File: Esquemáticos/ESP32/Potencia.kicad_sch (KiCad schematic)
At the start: 12 parts, among them J3 Barrel_Jack, SW1 SW_DIP_x01, U5 AMS1117-5.0, U6 AMS1117-3.3

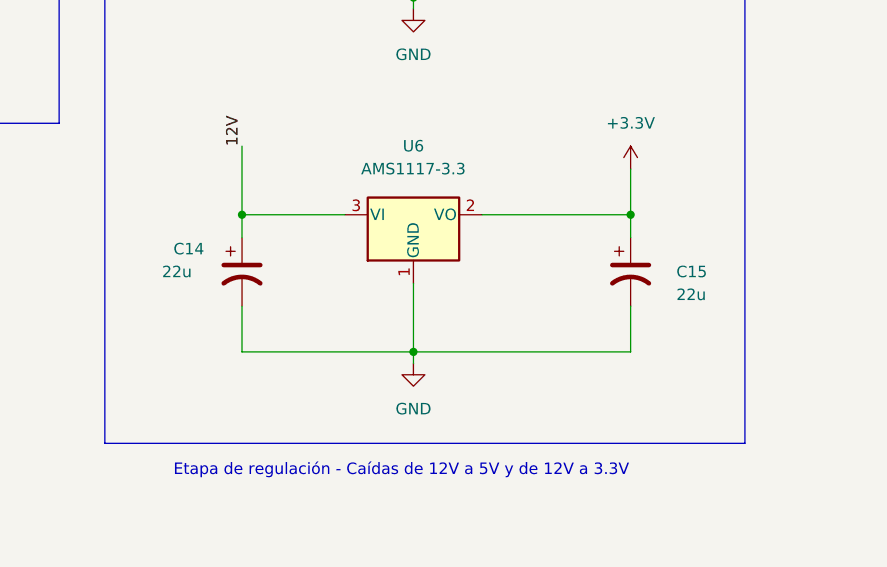
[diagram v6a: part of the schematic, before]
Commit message: Ruteo y zonas de cobre. Modo_serio.jpg
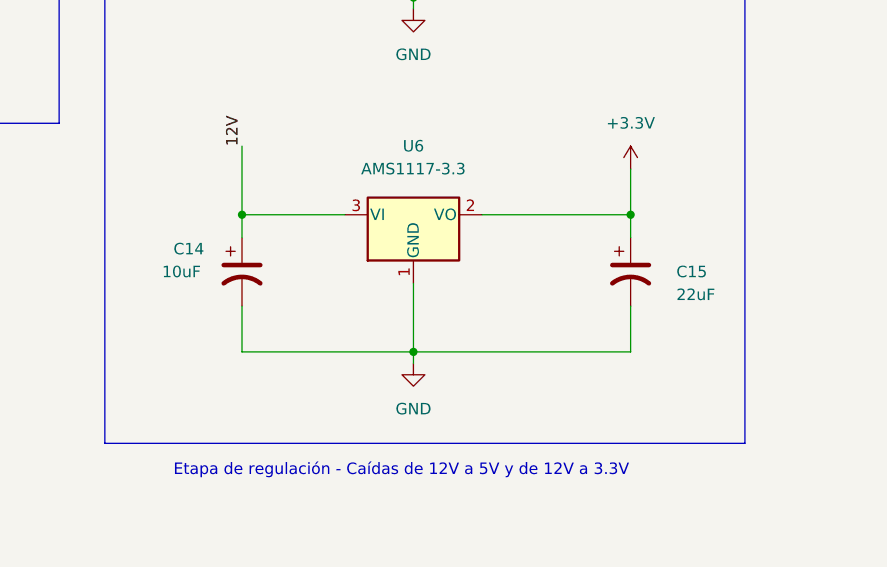
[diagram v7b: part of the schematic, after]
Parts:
- C14: value 22u -> 10uF
- C15: value 22u -> 22uF
- D3: footprint Diode_THT:D_DO-41_SOD81_P10.16mm_Horizontal -> Diode_SMD:D_SMA_Handsoldering
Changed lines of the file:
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@@
     (property "Reference" "D3" (id 0) (at 109.22 82.55 0))
     (property "Value" "1N4007" (id 1) (at 109.22 85.09 0))
-    (property "Footprint" "Diode_THT:D_DO-41_SOD81_P10.16mm_Horizontal" (id 2) (at 109.22 84.455 0)
+    (property "Footprint" "Diode_SMD:D_SMA_Handsoldering" (id 2) (at 109.22 84.455 0)
       (effects (font (size 1.27 1.27)) hide)
     )
@@
       (effects (font (size 1.27 1.27)) (justify left))
     )
-    (property "Value" "22u" (id 1) (at 212.09 137.16 0)
+    (property "Value" "22uF" (id 1) (at 212.09 137.16 0)
       (effects (font (size 1.27 1.27)) (justify left))
     )
@@
       (effects (font (size 1.27 1.27)) (justify left))
     )
-    (property "Value" "22u" (id 1) (at 154.94 134.62 0)
+    (property "Value" "10uF" (id 1) (at 154.94 134.62 0)
       (effects (font (size 1.27 1.27)) (justify left))
     )

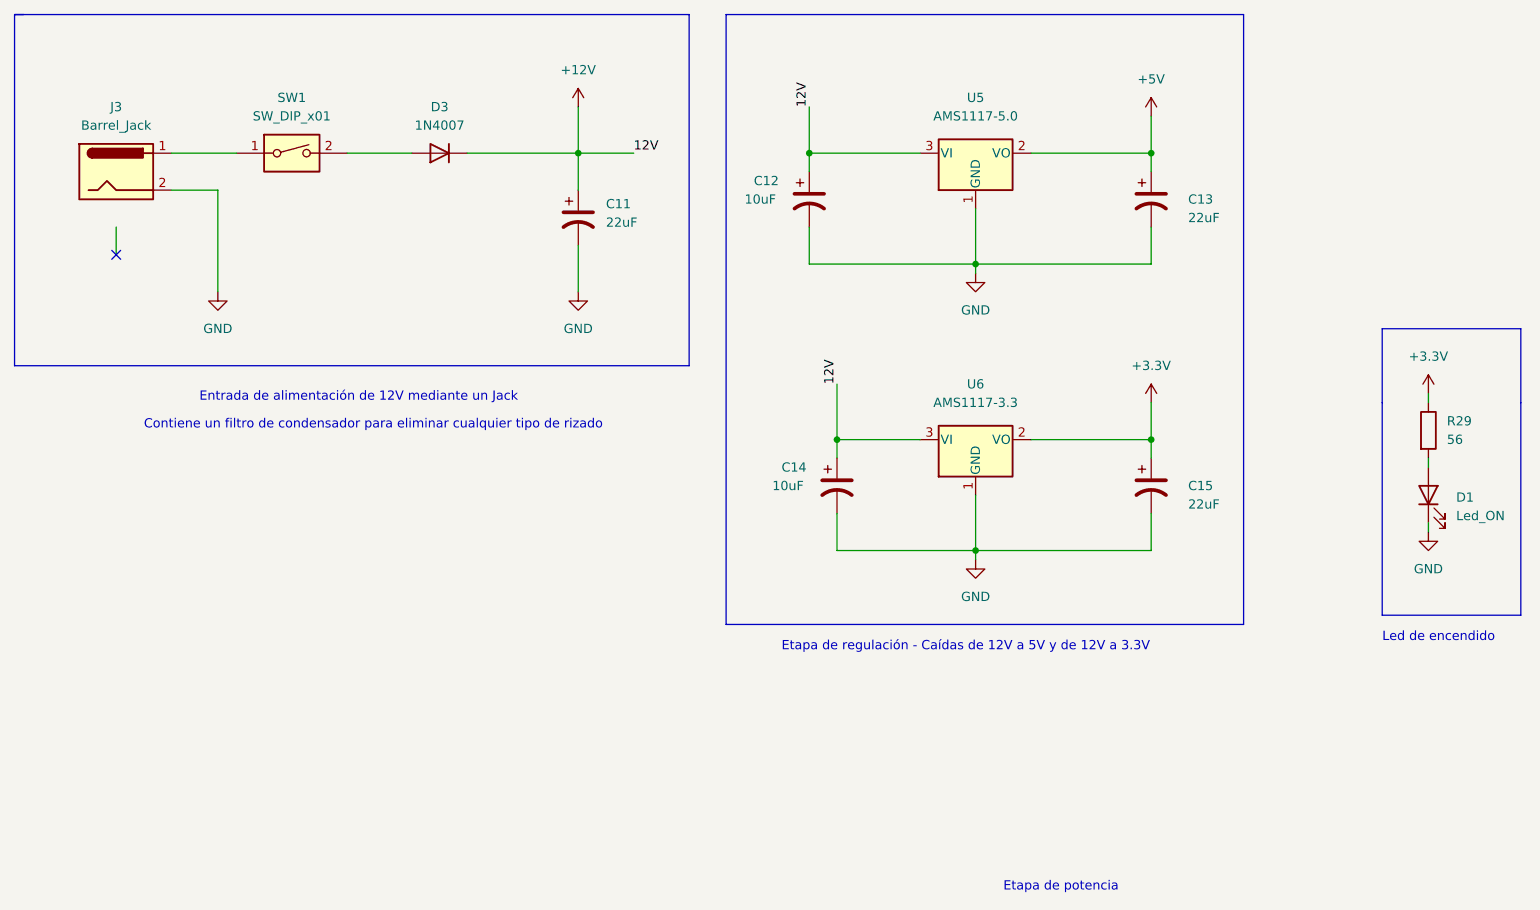
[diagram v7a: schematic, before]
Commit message: Huellas actualizadas según los vendedores locales
Falta la del optoacoplador y actualizar la placa. Además, dependiendo de la resñpuesta del profe tocaría re-diseñar todo :c
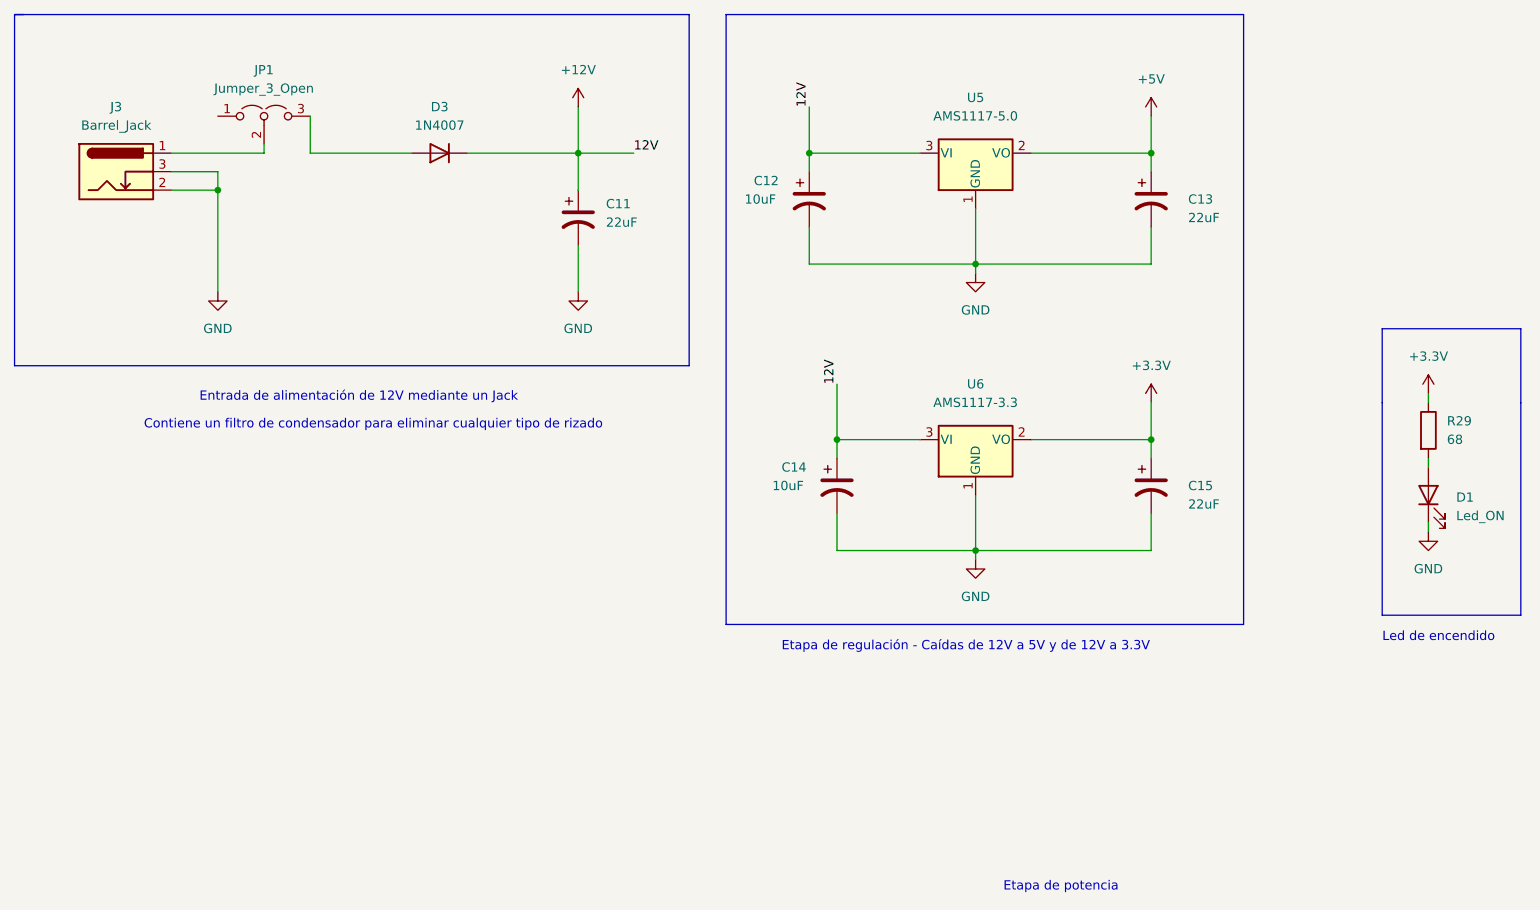
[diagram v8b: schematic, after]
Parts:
- removed SW1: SW_DIP_x01, Button_Switch_SMD:SW_DIP_SPSTx01_Slide_6.7x4.1mm_W6.73mm_P2.54mm_LowProfile_JPin, symbol Switch:SW_DIP_x01
- added JP1: Jumper_3_Open, Connector_PinHeader_2.54mm:PinHeader_1x03_P2.54mm_Vertical, symbol Jumper:Jumper_3_Open
- C11, C12, C13, C14, C15: footprint Capacitor_SMD:C_0603_1608Metric_Pad1.08x0.95mm_HandSolder -> Capacitor_SMD:C_0805_2012Metric_Pad1.18x1.45mm_HandSolder
- J3: footprint Connector_BarrelJack:BarrelJack_CLIFF_FC681465S_SMT_Horizontal -> Connector_BarrelJack:BarrelJack_GCT_DCJ200-10-A_Horizontal; symbol Connector:Barrel_Jack -> Connector:Barrel_Jack_Switch
- R29: value 56 -> 68; footprint Resistor_SMD:R_0603_1608Metric_Pad0.98x0.95mm_HandSolder -> Resistor_SMD:R_1206_3216Metric_Pad1.30x1.75mm_HandSolder
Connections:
- net GND: now also J3.3
- net at J3.1: now also JP1.2 (C)
- net at D3.2 (A): now also JP1.3 (B)
- no-connect marks 1 -> 0
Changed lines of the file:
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@@
 (kicad_sch (version 20211123) (generator eeschema)
   (paper "A4")
+  (junction (at 78.74 93.98) (diameter 0) (color 0 0 0 0)
+  )
   (junction (at 160.02 88.9) (diameter 0) (color 0 0 0 0)
   )
@@
   (junction (at 182.88 104.14) (diameter 0) (color 0 0 0 0)
   )
-  (no_connect (at 64.77 102.87))
   (wire (pts (xy 182.88 104.14) (xy 207.01 104.14))
     (stroke (width 0) (type default) (color 0 0 0 0))
@@
     (stroke (width 0) (type default) (color 0 0 0 0))
   )
-  (wire (pts (xy 72.39 88.9) (xy 81.28 88.9))
+  (wire (pts (xy 72.39 88.9) (xy 85.09 88.9))
     (stroke (width 0) (type default) (color 0 0 0 0))
   )
@@
     (stroke (width 0) (type default) (color 0 0 0 0))
   )
+  (wire (pts (xy 91.44 83.82) (xy 91.44 88.9))
+    (stroke (width 0) (type default) (color 0 0 0 0))
+  )
   (wire (pts (xy 245.11 130.81) (xy 245.11 132.08))
     (stroke (width 0) (type default) (color 0 0 0 0))
@@
     (stroke (width 0) (type default) (color 0 0 0 0))
   )
-  (wire (pts (xy 64.77 102.87) (xy 64.77 99.06))
-    (stroke (width 0) (type default) (color 0 0 0 0))
-  )
   (polyline (pts (xy 219.71 153.67) (xy 219.71 69.85))
     (stroke (width 0) (type default) (color 0 0 0 0))
@@
     (stroke (width 0) (type default) (color 0 0 0 0))
   )
+  (wire (pts (xy 85.09 87.63) (xy 85.09 88.9))
+    (stroke (width 0) (type default) (color 0 0 0 0))
+  )
   (wire (pts (xy 245.11 139.7) (xy 245.11 140.97))
     (stroke (width 0) (type default) (color 0 0 0 0))
@@
     (stroke (width 0) (type default) (color 0 0 0 0))
   )
-  (wire (pts (xy 96.52 88.9) (xy 105.41 88.9))
+  (wire (pts (xy 91.44 88.9) (xy 105.41 88.9))
     (stroke (width 0) (type default) (color 0 0 0 0))
   )
@@
     (stroke (width 0) (type default) (color 0 0 0 0))
   )
+  (wire (pts (xy 72.39 91.44) (xy 78.74 91.44))
+    (stroke (width 0) (type default) (color 0 0 0 0))
+  )
   (polyline (pts (xy 238.76 113.03) (xy 257.81 113.03))
     (stroke (width 0) (type default) (color 0 0 0 0))
@@
   )
   (polyline (pts (xy 257.81 113.03) (xy 257.81 123.19))
+    (stroke (width 0) (type default) (color 0 0 0 0))
+  )
+  (wire (pts (xy 78.74 91.44) (xy 78.74 93.98))
     (stroke (width 0) (type default) (color 0 0 0 0))
   )
@@
       (effects (font (size 1.27 1.27)) (justify left))
     )
-    (property "Footprint" "Capacitor_SMD:C_0603_1608Metric_Pad1.08x0.95mm_HandSolder" (id 2) (at 207.01 95.25 0)
+    (property "Footprint" "Capacitor_SMD:C_0805_2012Metric_Pad1.18x1.45mm_HandSolder" (id 2) (at 207.01 95.25 0)
       (effects (font (size 1.27 1.27)) hide)
     )
@@
       (effects (font (size 1.27 1.27)) (justify left))
     )
-    (property "Footprint" "Capacitor_SMD:C_0603_1608Metric_Pad1.08x0.95mm_HandSolder" (id 2) (at 160.02 95.25 0)
+    (property "Footprint" "Capacitor_SMD:C_0805_2012Metric_Pad1.18x1.45mm_HandSolder" (id 2) (at 160.02 95.25 0)
       (effects (font (size 1.27 1.27)) hide)
     )
@@
     (pin "2")
   )
-  (symbol (lib_id "Connector:Barrel_Jack") (at 64.77 91.44 0) (unit 1)
+  (symbol (lib_id "Connector:Barrel_Jack_Switch") (at 64.77 91.44 0) (unit 1)
     (in_bom yes) (on_board yes) (fields_autoplaced)
     (property "Reference" "J3" (id 0) (at 64.77 82.55 0))
     (property "Value" "Barrel_Jack" (id 1) (at 64.77 85.09 0))
-    (property "Footprint" "Connector_BarrelJack:BarrelJack_CLIFF_FC681465S_SMT_Horizontal" (id 2) (at 66.04 92.456 0)
+    (property "Footprint" "Connector_BarrelJack:BarrelJack_GCT_DCJ200-10-A_Horizontal" (id 2) (at 66.04 92.456 0)
       (effects (font (size 1.27 1.27)) hide)
     )
@@
     (pin "1")
     (pin "2")
+    (pin "3")
   )
   (symbol (lib_id "Diode:1N4007") (at 109.22 88.9 180) (unit 1)
@@
       (effects (font (size 1.27 1.27)) (justify left))
     )
-    (property "Footprint" "Capacitor_SMD:C_0603_1608Metric_Pad1.08x0.95mm_HandSolder" (id 2) (at 207.01 134.62 0)
+    (property "Footprint" "Capacitor_SMD:C_0805_2012Metric_Pad1.18x1.45mm_HandSolder" (id 2) (at 207.01 134.62 0)
       (effects (font (size 1.27 1.27)) hide)
     )
@@
       (effects (font (size 1.27 1.27)) (justify left))
     )
-    (property "Footprint" "Capacitor_SMD:C_0603_1608Metric_Pad1.08x0.95mm_HandSolder" (id 2) (at 163.83 134.62 0)
+    (property "Footprint" "Capacitor_SMD:C_0805_2012Metric_Pad1.18x1.45mm_HandSolder" (id 2) (at 163.83 134.62 0)
       (effects (font (size 1.27 1.27)) hide)
     )
@@
       (effects (font (size 1.27 1.27)) (justify left))
     )
-    (property "Footprint" "Capacitor_SMD:C_0603_1608Metric_Pad1.08x0.95mm_HandSolder" (id 2) (at 128.27 97.79 0)
+    (property "Footprint" "Capacitor_SMD:C_0805_2012Metric_Pad1.18x1.45mm_HandSolder" (id 2) (at 128.27 97.79 0)
       (effects (font (size 1.27 1.27)) hide)
     )
@@
     (pin "1")
   )
+  (symbol (lib_id "Jumper:Jumper_3_Open") (at 85.09 83.82 0) (unit 1)
+    (in_bom yes) (on_board yes) (fields_autoplaced)
+    (property "Reference" "JP1" (id 0) (at 85.09 77.47 0))
+    (property "Value" "Jumper_3_Open" (id 1) (at 85.09 80.01 0))
+    (property "Footprint" "Connector_PinHeader_2.54mm:PinHeader_1x03_P2.54mm_Vertical" (id 2) (at 85.09 83.82 0)
+      (effects (font (size 1.27 1.27)) hide)
+    )
+    (property "Datasheet" "~" (id 3) (at 85.09 83.82 0)
+      (effects (font (size 1.27 1.27)) hide)
+    )
+    (pin "1")
+    (pin "2")
+    (pin "3")
+  )
   (symbol (lib_id "Device:R") (at 245.11 127 0) (unit 1)
     (in_bom yes) (on_board yes) (fields_autoplaced)
@@
       (effects (font (size 1.27 1.27)) (justify left))
     )
-    (property "Value" "56" (id 1) (at 247.65 128.2699 0)
-      (effects (font (size 1.27 1.27)) (justify left))
-    )
-    (property "Footprint" "Resistor_SMD:R_0603_1608Metric_Pad0.98x0.95mm_HandSolder" (id 2) (at 243.332 127 90)
+    (property "Value" "68" (id 1) (at 247.65 128.2699 0)
+      (effects (font (size 1.27 1.27)) (justify left))
+    )
+    (property "Footprint" "Resistor_SMD:R_1206_3216Metric_Pad1.30x1.75mm_HandSolder" (id 2) (at 243.332 127 90)
       (effects (font (size 1.27 1.27)) hide)
     )
@@
       (effects (font (size 1.27 1.27)) hide)
     )
-    (pin "1")
-    (pin "2")
-  )
-  (symbol (lib_id "Switch:SW_DIP_x01") (at 88.9 88.9 0) (unit 1)
-    (in_bom yes) (on_board yes) (fields_autoplaced)
-    (property "Reference" "SW1" (id 0) (at 88.9 81.28 0))
-    (property "Value" "SW_DIP_x01" (id 1) (at 88.9 83.82 0))
-    (property "Footprint" "Button_Switch_SMD:SW_DIP_SPSTx01_Slide_6.7x4.1mm_W6.73mm_P2.54mm_LowProfile_JPin" (id 2) (at 88.9 88.9 0)
-      (effects (font (size 1.27 1.27)) hide)
-    )
-    (property "Datasheet" "~" (id 3) (at 88.9 88.9 0)
-      (effects (font (size 1.27 1.27)) hide)
-    )
